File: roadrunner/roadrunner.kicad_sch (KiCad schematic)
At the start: 82 parts, among them J1 Battery_conn, J2 battery_conn_r, J4 niceview_left, J5 niceview_right, SW1 SW_Push, SW10 SW_Push, SW10_r1 SW_Push, SW11 SW_Push, SW11_r1 SW_Push, SW12 SW_Push, SW12_r1 SW_Push, SW13 SW_Push, SW13_r1 SW_Push, SW14 SW_Push, SW14_r1 SW_Push, SW15 SW_Push, SW15_r1 SW_Push, SW16 SW_Push, SW16_r1 SW_Push, SW17 SW_Push, SW17_r1 SW_Push, SW1_r1 SW_Push, SW2 SW_Push, SW2_r1 SW_Push, SW3 SW_Push, SW3_r1 SW_Push, SW4 SW_Push, SW4_r1 SW_Push, SW5 SW_Push, SW5_r1 SW_Push, SW6 SW_Push, SW6_r1 SW_Push, SW7 SW_Push, SW7_r1 SW_Push, SW8 SW_Push, SW8_r1 SW_Push, SW9 SW_Push, SW9_r1 SW_Push, U1 ProMicro-kbd, U2 ProMicro-kbd

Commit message: place diodes
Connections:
- net COL0: now also SW1.1
- net COL2_r: now also SW3_r1.1
- net COL3_r: now also SW2_r1.1
- net COL4_r: now also SW1_r1.1
- net ROW0_r: now also D20.1 (K)
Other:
- moved on the sheet: D20
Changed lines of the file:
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@@
   (junction (at 110.49 87.63) (diameter 0) (color 0 0 0 0)
   )
+  (junction (at 267.97 92.71) (diameter 0) (color 0 0 0 0)
+  )
   (junction (at 265.43 124.46) (diameter 0) (color 0 0 0 0)
   )
@@
   (junction (at 232.41 124.46) (diameter 0) (color 0 0 0 0)
   )
+  (junction (at 35.56 88.9) (diameter 0) (color 0 0 0 0)
+  )
   (junction (at 236.22 133.35) (diameter 0) (color 0 0 0 0)
   )
@@
   (junction (at 92.71 87.63) (diameter 0) (color 0 0 0 0)
   )
+  (junction (at 236.22 114.3) (diameter 0) (color 0 0 0 0)
+  )
+  (junction (at 231.14 168.91) (diameter 0) (color 0 0 0 0)
+  )
+  (junction (at 87.63 104.14) (diameter 0) (color 0 0 0 0)
+  )
+  (junction (at 236.22 92.71) (diameter 0) (color 0 0 0 0)
+  )
+  (junction (at 48.26 124.46) (diameter 0) (color 0 0 0 0)
+  )
+  (junction (at 110.49 114.3) (diameter 0) (color 0 0 0 0)
+  )
+  (junction (at 87.63 124.46) (diameter 0) (color 0 0 0 0)
+  )
   (junction (at 265.43 104.14) (diameter 0) (color 0 0 0 0)
   )
-  (junction (at 236.22 114.3) (diameter 0) (color 0 0 0 0)
-  )
-  (junction (at 231.14 168.91) (diameter 0) (color 0 0 0 0)
-  )
-  (junction (at 87.63 104.14) (diameter 0) (color 0 0 0 0)
-  )
-  (junction (at 236.22 92.71) (diameter 0) (color 0 0 0 0)
-  )
-  (junction (at 48.26 124.46) (diameter 0) (color 0 0 0 0)
-  )
-  (junction (at 110.49 114.3) (diameter 0) (color 0 0 0 0)
-  )
-  (junction (at 87.63 124.46) (diameter 0) (color 0 0 0 0)
-  )
   (junction (at 87.63 146.05) (diameter 0) (color 0 0 0 0)
   )
@@
   (junction (at 35.56 114.3) (diameter 0) (color 0 0 0 0)
   )
+  (junction (at 252.73 92.71) (diameter 0) (color 0 0 0 0)
+  )
   (junction (at 280.67 124.46) (diameter 0) (color 0 0 0 0)
   )
@@
   (junction (at 49.53 104.14) (diameter 0) (color 0 0 0 0)
   )
+  (junction (at 283.21 92.71) (diameter 0) (color 0 0 0 0)
+  )
   (junction (at 218.44 92.71) (diameter 0) (color 0 0 0 0)
   )
@@
   (junction (at 267.97 114.3) (diameter 0) (color 0 0 0 0)
   )
-  (junction (at 265.43 93.9196) (diameter 0) (color 0 0 0 0)
-  )
   (junction (at 105.41 104.14) (diameter 0) (color 0 0 0 0)
   )
@@
     (stroke (width 0) (type default) (color 0 0 0 0))
   )
+  (wire (pts (xy 283.21 92.71) (xy 285.75 92.71))
+    (stroke (width 0) (type default) (color 0 0 0 0))
+  )
   (wire (pts (xy 247.65 142.24) (xy 247.65 144.78))
     (stroke (width 0) (type default) (color 0 0 0 0))
@@
     (stroke (width 0) (type default) (color 0 0 0 0))
   )
-  (wire (pts (xy 280.67 104.14) (xy 265.43 104.14))
-    (stroke (width 0) (type default) (color 0 0 0 0))
-  )
   (wire (pts (xy 252.73 133.35) (xy 254 133.35))
     (stroke (width 0) (type default) (color 0 0 0 0))
@@
     (stroke (width 0) (type default) (color 0 0 0 0))
   )
+  (wire (pts (xy 283.21 92.71) (xy 283.21 114.3))
+    (stroke (width 0) (type default) (color 0 0 0 0))
+  )
   (polyline (pts (xy 364.49 187.96) (xy 203.2 187.96))
     (stroke (width 0) (type default) (color 0 0 0 0))
@@
     (stroke (width 0) (type default) (color 0 0 0 0))
   )
+  (wire (pts (xy 35.56 88.9) (xy 39.37 88.9))
+    (stroke (width 0) (type default) (color 0 0 0 0))
+  )
   (wire (pts (xy 87.63 88.9) (xy 87.63 91.44))
     (stroke (width 0) (type default) (color 0 0 0 0))
@@
     (stroke (width 0) (type default) (color 0 0 0 0))
   )
+  (wire (pts (xy 265.43 104.14) (xy 280.67 104.14))
+    (stroke (width 0) (type default) (color 0 0 0 0))
+  )
+  (wire (pts (xy 252.73 92.71) (xy 252.73 114.3))
+    (stroke (width 0) (type default) (color 0 0 0 0))
+  )
   (wire (pts (xy 295.91 124.46) (xy 280.67 124.46))
     (stroke (width 0) (type default) (color 0 0 0 0))
@@
     (stroke (width 0) (type default) (color 0 0 0 0))
   )
-  (wire (pts (xy 267.97 83.82) (xy 267.97 114.3))
+  (wire (pts (xy 267.97 83.82) (xy 267.97 92.71))
     (stroke (width 0) (type default) (color 0 0 0 0))
   )
@@
     (stroke (width 0) (type default) (color 0 0 0 0))
   )
+  (wire (pts (xy 265.43 102.87) (xy 265.43 104.14))
+    (stroke (width 0) (type default) (color 0 0 0 0))
+  )
   (wire (pts (xy 69.85 88.9) (xy 69.85 91.44))
     (stroke (width 0) (type default) (color 0 0 0 0))
@@
     (stroke (width 0) (type default) (color 0 0 0 0))
   )
-  (wire (pts (xy 283.21 83.82) (xy 283.21 114.3))
+  (wire (pts (xy 283.21 83.82) (xy 283.21 92.71))
     (stroke (width 0) (type default) (color 0 0 0 0))
   )
@@
     (stroke (width 0) (type default) (color 0 0 0 0))
   )
+  (wire (pts (xy 267.97 92.71) (xy 267.97 114.3))
+    (stroke (width 0) (type default) (color 0 0 0 0))
+  )
   (wire (pts (xy 231.14 144.78) (xy 215.9 144.78))
     (stroke (width 0) (type default) (color 0 0 0 0))
@@
     (stroke (width 0) (type default) (color 0 0 0 0))
   )
-  (wire (pts (xy 265.43 104.14) (xy 248.92 104.14))
+  (wire (pts (xy 248.92 104.14) (xy 265.43 104.14))
     (stroke (width 0) (type default) (color 0 0 0 0))
   )
@@
     (stroke (width 0) (type default) (color 0 0 0 0))
   )
+  (wire (pts (xy 252.73 92.71) (xy 255.27 92.71))
+    (stroke (width 0) (type default) (color 0 0 0 0))
+  )
   (wire (pts (xy 124.46 123.19) (xy 124.46 124.46))
     (stroke (width 0) (type default) (color 0 0 0 0))
@@
     (stroke (width 0) (type default) (color 0 0 0 0))
   )
+  (wire (pts (xy 35.56 88.9) (xy 35.56 114.3))
+    (stroke (width 0) (type default) (color 0 0 0 0))
+  )
   (wire (pts (xy 295.91 101.6) (xy 295.91 104.14))
     (stroke (width 0) (type default) (color 0 0 0 0))
@@
     (stroke (width 0) (type default) (color 0 0 0 0))
   )
-  (wire (pts (xy 265.43 101.6) (xy 265.43 104.14))
-    (stroke (width 0) (type default) (color 0 0 0 0))
-  )
   (wire (pts (xy 55.88 88.9) (xy 59.69 88.9))
     (stroke (width 0) (type default) (color 0 0 0 0))
@@
     (stroke (width 0) (type default) (color 0 0 0 0))
   )
-  (wire (pts (xy 265.43 92.71) (xy 265.43 93.9196))
-    (stroke (width 0) (type default) (color 0 0 0 0))
-  )
   (wire (pts (xy 106.68 165.1) (xy 106.68 166.37))
     (stroke (width 0) (type default) (color 0 0 0 0))
@@
     (stroke (width 0) (type default) (color 0 0 0 0))
   )
-  (wire (pts (xy 35.56 86.36) (xy 35.56 114.3))
+  (wire (pts (xy 35.56 86.36) (xy 35.56 88.9))
     (stroke (width 0) (type default) (color 0 0 0 0))
   )
@@
     (stroke (width 0) (type default) (color 0 0 0 0))
   )
-  (wire (pts (xy 252.73 85.09) (xy 252.73 114.3))
+  (wire (pts (xy 252.73 85.09) (xy 252.73 92.71))
     (stroke (width 0) (type default) (color 0 0 0 0))
   )
@@
     (stroke (width 0) (type default) (color 0 0 0 0))
   )
-  (wire (pts (xy 265.43 93.9196) (xy 265.43 93.98))
-    (stroke (width 0) (type default) (color 0 0 0 0))
-  )
   (wire (pts (xy 110.49 85.09) (xy 110.49 87.63))
     (stroke (width 0) (type default) (color 0 0 0 0))
@@
   )
   (wire (pts (xy 105.41 114.3) (xy 105.41 115.57))
+    (stroke (width 0) (type default) (color 0 0 0 0))
+  )
+  (wire (pts (xy 267.97 92.71) (xy 270.51 92.71))
+    (stroke (width 0) (type default) (color 0 0 0 0))
+  )
+  (wire (pts (xy 265.43 92.71) (xy 265.43 95.25))
     (stroke (width 0) (type default) (color 0 0 0 0))
   )
@@
     (pin "2")
   )
-  (symbol (lib_id "Diode:1N4148W") (at 265.43 97.7296 90) (unit 1)
+  (symbol (lib_id "Diode:1N4148W") (at 265.43 99.06 90) (unit 1)
     (in_bom yes) (on_board yes)
-    (property "Reference" "D20" (id 0) (at 259.08 97.7296 90)
+    (property "Reference" "D20" (id 0) (at 259.08 99.06 90)
       (effects (font (size 1.27 1.27)) (justify right))
     )
-    (property "Value" "1N4148W" (id 1) (at 254 100.2696 90)
+    (property "Value" "1N4148W" (id 1) (at 254 101.6 90)
       (effects (font (size 1.27 1.27)) (justify right))
     )
-    (property "Footprint" "Diode_SMD:D_SOD-123" (id 2) (at 269.875 97.7296 0)
-      (effects (font (size 1.27 1.27)) hide)
-    )
-    (property "Datasheet" "https://www.vishay.com/docs/85748/1n4148w.pdf" (id 3) (at 265.43 97.7296 0)
-      (effects (font (size 1.27 1.27)) hide)
-    )
+    (property "Footprint" "Diode_SMD:D_SOD-123" (id 2) (at 269.875 99.06 0)
+      (effects (font (size 1.27 1.27)) hide)
+    )
+    (property "Datasheet" "https://www.vishay.com/docs/85748/1n4148w.pdf" (id 3) (at 265.43 99.06 0)
+      (effects (font (size 1.27 1.27)) hide)
+    )

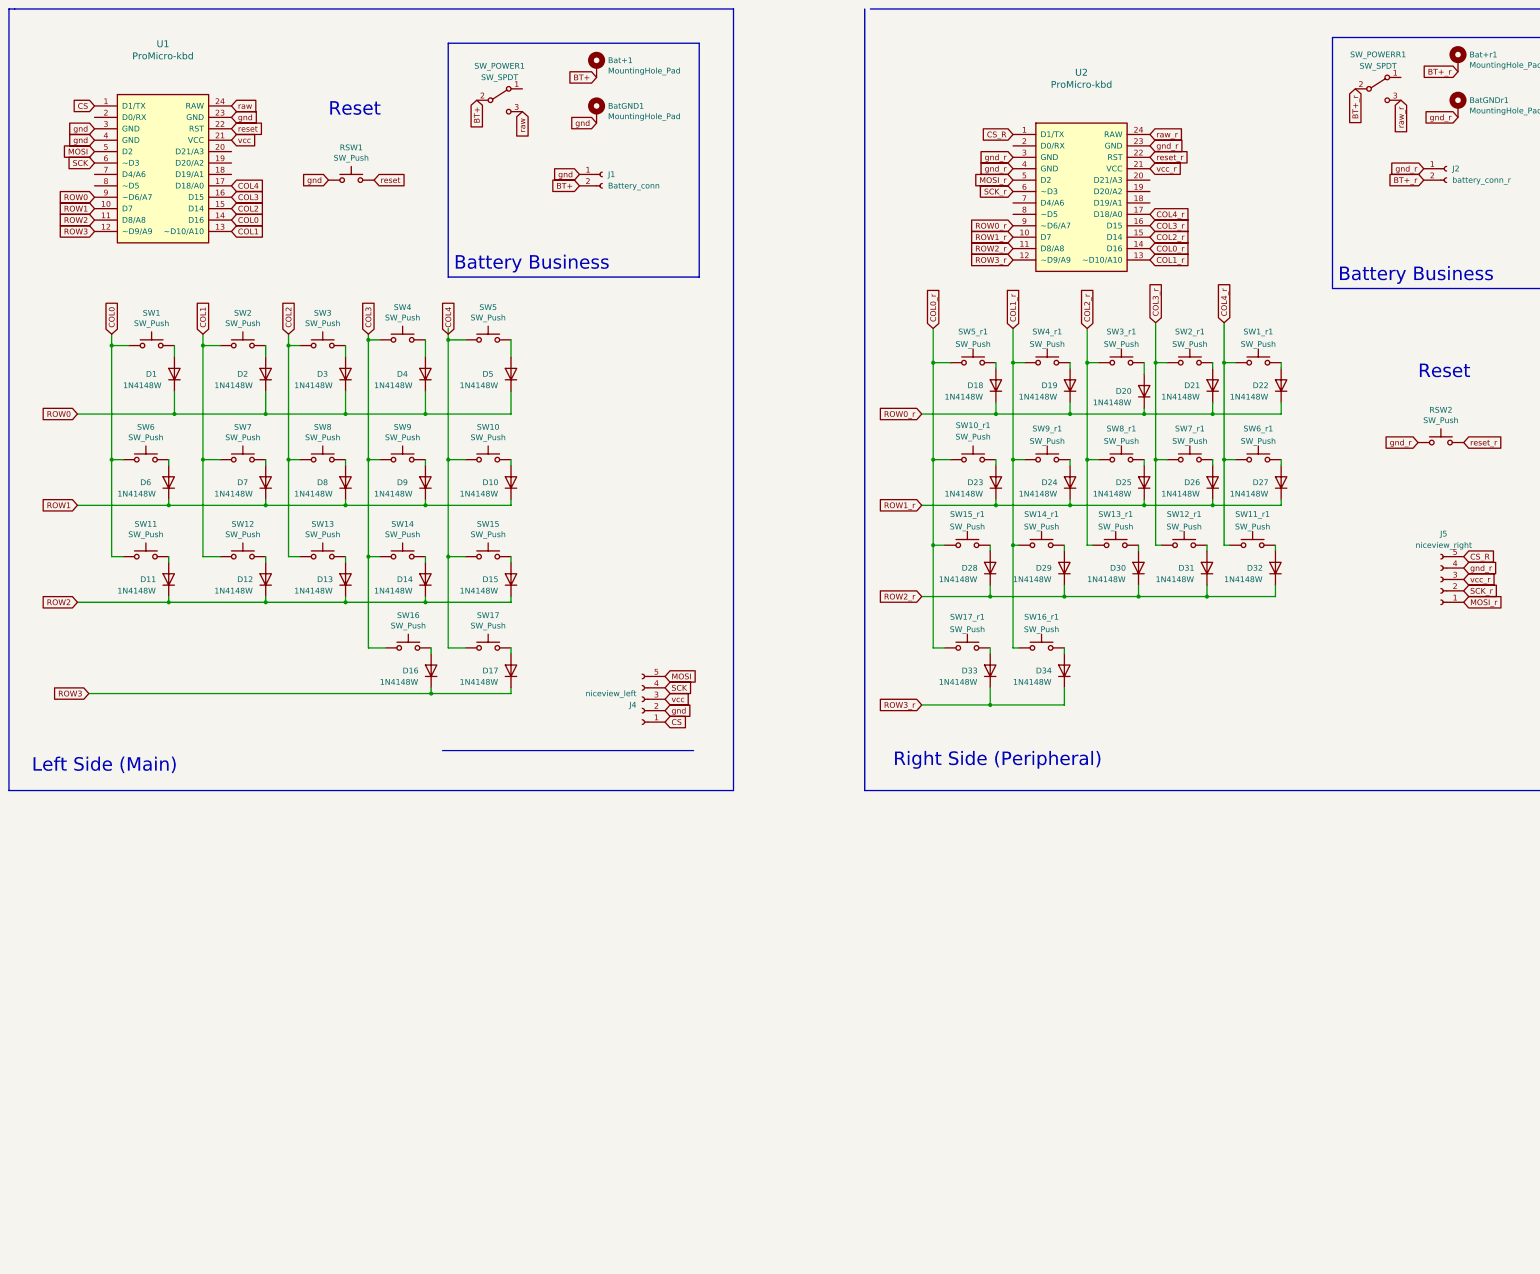
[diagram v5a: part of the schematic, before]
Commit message: begin adding mouse
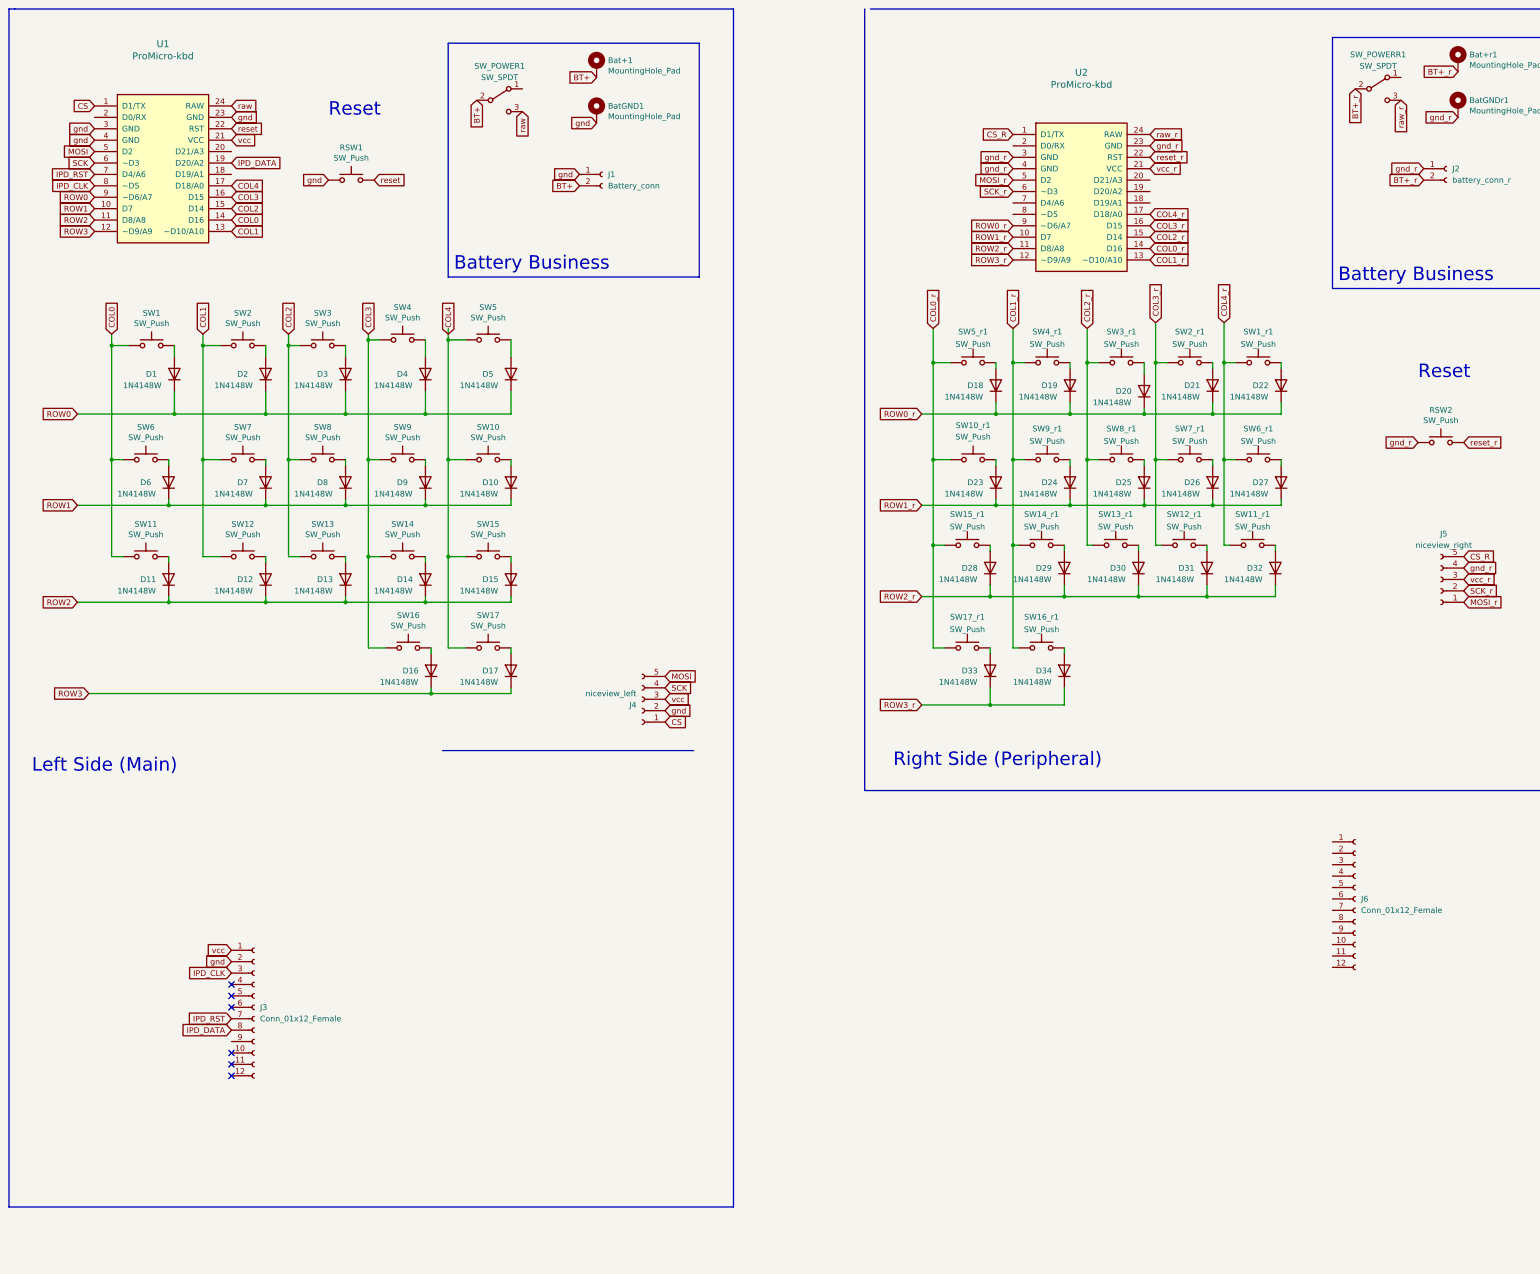
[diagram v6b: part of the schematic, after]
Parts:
- added J3: Conn_01x12_Female, Connector_FFC-FPC:Hirose_FH12-12S-0.5SH_1x12-1MP_P0.50mm_Horizontal, symbol Connector:Conn_01x12_Female
- added J6: Conn_01x12_Female, symbol Connector:Conn_01x12_Female
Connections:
- net gnd: now also J3.2 (Pin_2)
- net vcc: now also J3.1 (Pin_1)
- net IPD_DATA: now reaches U1.19 (D20/A2)
- net IPD_DATA: now also J3.8 (Pin_8)
- net IPD_RST: now reaches U1.7 (D4/A6)
- net IPD_RST: now also J3.7 (Pin_7)
- net IPD_CLK: now reaches U1.8 (~D5)
- net IPD_CLK: now also J3.3 (Pin_3)
- no-connect marks 0 -> 6

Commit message: feat: add vik
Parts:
- added J7: VIK_Left, Connector_FFC-FPC:Hirose_FH12-12S-0.5SH_1x12-1MP_P0.50mm_Horizontal, symbol Connector:Conn_01x12_Socket
- added J8: VIK_Right, Connector_FFC-FPC:Hirose_FH12-12S-0.5SH_1x12-1MP_P0.50mm_Horizontal, symbol Connector:Conn_01x12_Socket
- J3: value Conn_01x12_Female -> track_point_left; footprint Connector_FFC-FPC:Hirose_FH12-12S-0.5SH_1x12-1MP_P0.50mm_Horizontal -> Connector_FFC-FPC:TE_1-84953-2_1x12-1MP_P1.0mm_Horizontal
- J6: value Conn_01x12_Female -> track_point_right; footprint (none) -> Connector_FFC-FPC:TE_1-84953-2_1x12-1MP_P1.0mm_Horizontal
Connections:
- net CS: now also J7.10 (Pin_10)
- net CS_R: no longer U2.1 (D1/TX)
- net IPD_CLK: now also J3.8 (Pin_8), J7.4 (Pin_4); no longer J3.3 (Pin_3)
- net IPD_DATA: now also J3.2 (Pin_2), U1.7 (D4/A6), J7.3 (Pin_3); no longer J3.8 (Pin_8), U1.19 (D20/A2)
- net IPD_RST: now also J3.3 (Pin_3), U1.19 (D20/A2), J7.5 (Pin_5); no longer J3.7 (Pin_7), U1.7 (D4/A6)
- net MOSI: now also J7.8 (Pin_8)
- net MOSI_r: now also J8.8 (Pin_8)
- net SCK: now also J7.12 (Pin_12)
- net SCK_r: now also J8.12 (Pin_12)
- net gnd: now also J3.7 (Pin_7), J7.2 (Pin_2); no longer J3.2 (Pin_2)
- net gnd_r: now also J6.7 (Pin_7), J8.2 (Pin_2)
- net vcc: now also J7.1 (Pin_1), J7.6 (Pin_6)
- net vcc_r: now also J6.1 (Pin_1), J8.1 (Pin_1), J8.6 (Pin_6)
- net GPIO1_r: now reaches U2.18 (D19/A1)
- net GPIO1_r: now also J8.7 (Pin_7)
- net IPD_RST_r: now reaches U2.19 (D20/A2)
- net IPD_RST_r: now also J6.3 (Pin_3), J8.5 (Pin_5)
- net MISO_r: now reaches U2.2 (D0/RX)
- net MISO_r: now also J8.11 (Pin_11)
- net GPIO2_r: now reaches U2.20 (D21/A3)
- net GPIO2_r: now also J8.9 (Pin_9)
- net IPD_DATA_r: now reaches U2.7 (D4/A6)
- net IPD_DATA_r: now also J6.2 (Pin_2), J8.3 (Pin_3)
- net IPD_CLK_r: now reaches U2.8 (~D5)
- net IPD_CLK_r: now also J6.8 (Pin_8), J8.4 (Pin_4)
- net GPIO1: now reaches U1.18 (D19/A1)
- net GPIO1: now also J7.7 (Pin_7)
- net MISO: now reaches U1.2 (D0/RX)
- net MISO: now also J7.11 (Pin_11)
- net GPIO2: now reaches U1.20 (D21/A3)
- net GPIO2: now also J7.9 (Pin_9)
- new net CS_r: J8.10 (Pin_10), U2.1 (D1/TX)
- no-connect marks 6 -> 14
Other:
- note added: "Battery"
- note added: "Nice!Nano"
- note added: "Peripherals"
- note removed: "Battery Business"
- moved on the sheet: Bat+1, BatGND1, D1, D10, D11, D12, D13, D14, D15, D16, D17, D18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

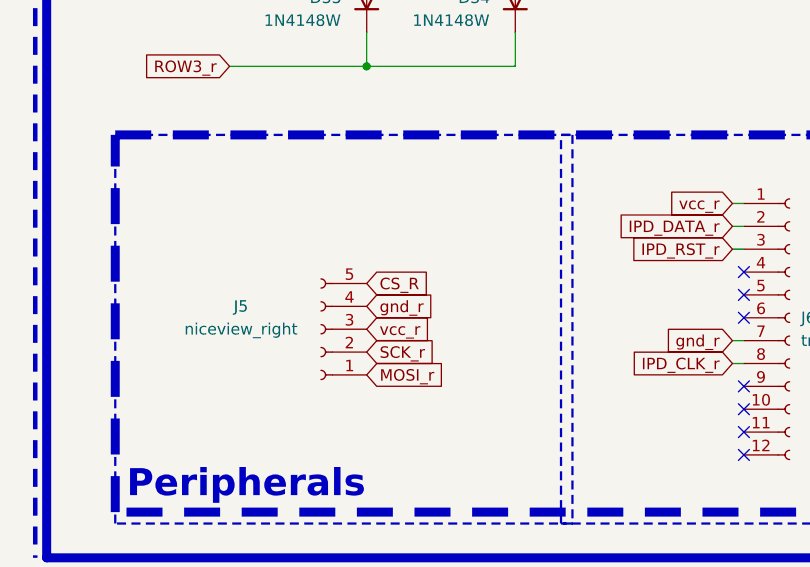
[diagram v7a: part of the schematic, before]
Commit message: chore: specify trackpoint model
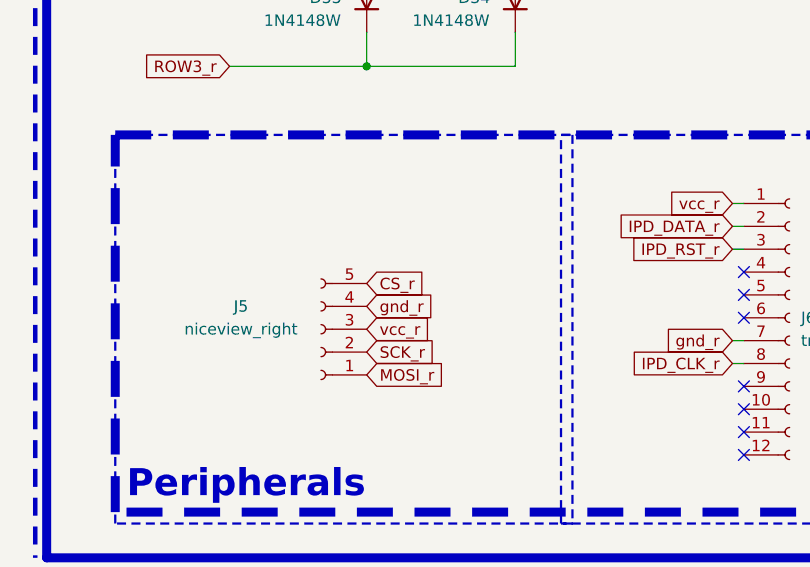
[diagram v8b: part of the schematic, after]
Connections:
- net CS_R is gone; now on net CS_r: J5.5 (Pin_5)
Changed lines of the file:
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@@
     )
   )
-  (global_label "CS_R" (shape input) (at 238.76 193.04 0) (fields_autoplaced)
+  (global_label "CS_r" (shape input) (at 238.76 193.04 0) (fields_autoplaced)
     (effects (font (size 1.27 1.27)) (justify left))
-    (property "Intersheetrefs" "${INTERSHEET_REFS}" (at 245.8902 193.1194 0)
+    (property "Intersheetrefs" "${INTERSHEET_REFS}" (at 245.9785 193.04 0)
       (effects (font (size 1.27 1.27)) (justify left) hide)
     )
